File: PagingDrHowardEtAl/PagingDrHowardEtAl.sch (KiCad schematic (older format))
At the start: 0 parts

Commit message: Complete PagingDrHowardEtAl
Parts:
- added P1: Pulse Playground, ~, symbol CONN_3
- added P2: 7 segment backpack, ~, symbol CONN_5
- added P3: Bargraph Backpack, ~, symbol CONN_4
- added U1: ITSYBITSY, ~, symbol ITSYBITSY
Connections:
- new net +: P2.3, U1.30 (Vhi)
- new net -: P1.3 (P3), P2.4, P3.3 (P3), U1.2 (G)
- new net C: P2.2, P3.1 (P1), U1.11 (SCL/3)
- new net D: P2.1, P3.2 (P2), U1.12 (SDA/2)
- new net IO: P1.1 (P1), P2.5, P3.4 (P4), U1.32 (3V)
- new net Pulse: P1.2 (PM), U1.29 (A0)
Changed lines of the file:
@@
 LIBS:feather_m0_express
 LIBS:metromini
+LIBS:itsybitsy
+LIBS:PagingDrHowardEtAl-cache
 EELAYER 27 0
 EELAYER END
@@
 Sheet 1 1
 Title ""
-Date "22 oct 2018"
+Date "5 nov 2018"
 Rev ""
 Comp ""
@@
 Comment4 ""
 $EndDescr
+$Comp
+L CONN_3 P1
+U 1 1 5BE04B98
+P 2050 3100
+F 0 "P1" V 2000 3100 50  0000 C CNN
+F 1 "Pulse Playground" V 2100 3100 40  0000 C CNN
+F 2 "~" H 2050 3100 60  0000 C CNN
+F 3 "~" H 2050 3100 60  0000 C CNN
+	1    2050 3100
+	-1   0    0    -1
+$EndComp
+$Comp
+L CONN_4 P3
+U 1 1 5BE04C5D
+P 5300 3700
+F 0 "P3" V 5250 3700 50  0000 C CNN
+F 1 "Bargraph Backpack" V 5350 3700 50  0000 C CNN
+F 2 "~" H 5300 3700 60  0000 C CNN
+F 3 "~" H 5300 3700 60  0000 C CNN
+	1    5300 3700
+	1    0    0    -1
+$EndComp
+$Comp
+L CONN_5 P2
+U 1 1 5BE05043
+P 5300 2450
+F 0 "P2" V 5250 2450 50  0000 C CNN
+F 1 "7 segment backpack" V 5350 2450 50  0000 C CNN
+F 2 "~" H 5300 2450 60  0000 C CNN
+F 3 "~" H 5300 2450 60  0000 C CNN
+	1    5300 2450
+	1    0    0    -1
+$EndComp
+Text Label 4900 2250 2    60   ~ 0
+D
+Text Label 4900 2350 2    60   ~ 0
+C
+Text Label 4900 2450 2    60   ~ 0
++
+Text Label 4900 2550 2    60   ~ 0
+-
+Text Label 4900 2650 2    60   ~ 0
+IO
+Text Label 4950 3550 2    60   ~ 0
+SCL
+Text Label 4950 3650 2    60   ~ 0
+SDA
+Text Label 4950 3750 2    60   ~ 0
+G
+Text Label 4950 3850 2    60   ~ 0
+Vcc
+Text Label 2400 3000 0    60   ~ 0
+Vdd
+Text Label 2400 3100 0    60   ~ 0
+Pulse
+Text Label 2400 3200 0    60   ~ 0
+GND
+$Comp
+L ITSYBITSY U1
+U 1 1 5BE053A3
+P 3700 2600
+F 0 "U1" H 3700 2900 60  0000 C CNN
+F 1 "ITSYBITSY" H 3650 2200 60  0000 C CNN
+F 2 "~" H 3700 2600 60  0000 C CNN
+F 3 "~" H 3700 2600 60  0000 C CNN
+	1    3700 2600
+	0    1    1    0
+$EndComp
+Wire Wire Line
+	2400 3000 2600 3000
+Wire Wire Line
+	2600 1400 2600 4500
+Wire Wire Line
+	2600 1400 2950 1400
+Wire Wire Line
+	2400 3200 2500 3200
+Wire Wire Line
+	2500 3200 2500 650
+Wire Wire Line
+	2500 650  4650 650
+Wire Wire Line
+	4650 650  4650 1200
+Wire Wire Line
+	4650 1200 4400 1200
+Wire Wire Line
+	2400 3100 2700 3100
+Wire Wire Line
+	2700 3100 2700 1850
+Wire Wire Line
+	2700 1850 2950 1850
+Wire Wire Line
+	4900 2250 4650 2250
+Wire Wire Line
+	4650 2250 4650 3650
+Wire Wire Line
+	4650 2700 4400 2700
+Wire Wire Line
+	4650 3650 4950 3650
+Connection ~ 4650 2700
+Wire Wire Line
+	4900 2350 4750 2350
+Wire Wire Line
+	4750 2350 4750 3550
+Wire Wire Line
+	4750 2550 4400 2550
+Wire Wire Line
+	4750 3550 4950 3550
+Connection ~ 4750 2550
+Wire Wire Line
+	4950 3750 4550 3750
+Wire Wire Line
+	4550 3750 4550 1200
+Connection ~ 4550 1200
+Wire Wire Line
+	4900 2550 4800 2550
+Wire Wire Line
+	4800 2550 4800 2850
+Wire Wire Line
+	4800 2850 4550 2850
+Connection ~ 4550 2850
+Wire Wire Line
+	4900 2650 4900 3500
+Wire Wire Line
+	4900 3500 4350 3500
+Wire Wire Line
+	4350 3500 4350 4500
+Wire Wire Line
+	4350 4500 2600 4500
+Connection ~ 2600 3000
+Wire Wire Line
+	4950 3850 4350 3850
+Connection ~ 4350 3850
+Wire Wire Line
+	4900 2450 4700 2450
+Wire Wire Line
+	4700 2450 4700 750
+Wire Wire Line
+	4700 750  2800 750
+Wire Wire Line
+	2800 750  2800 1700
+Wire Wire Line
+	2800 1700 2950 1700
 $EndSCHEMATC

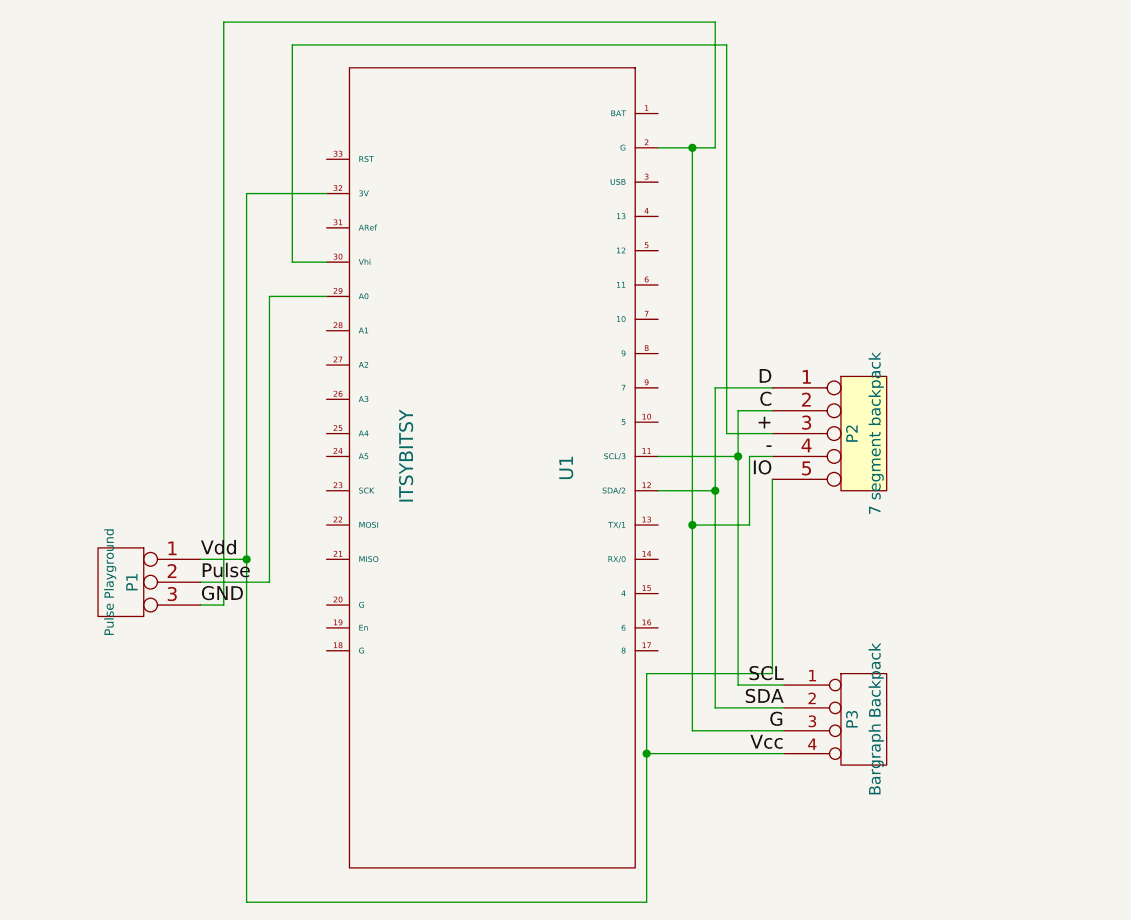
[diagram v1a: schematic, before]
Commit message: Add detailed comments to both the code and the schematics
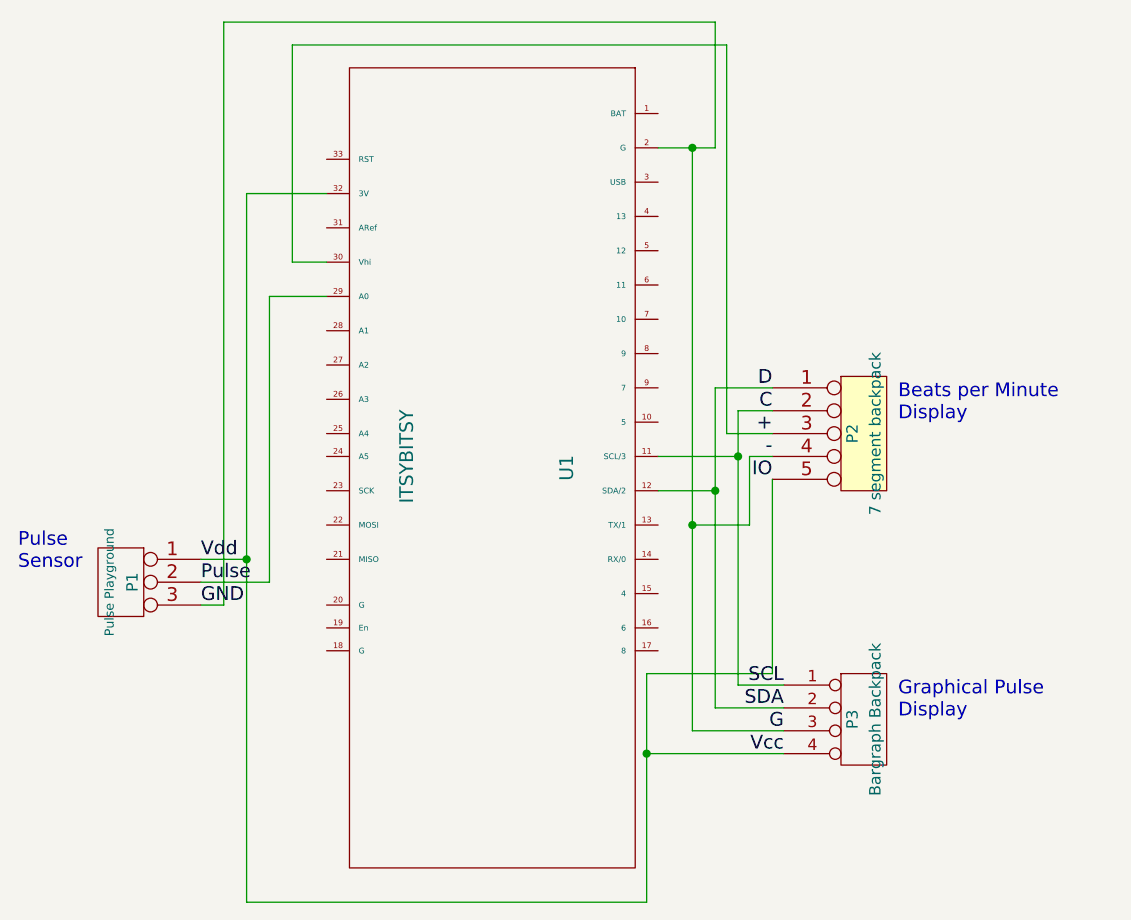
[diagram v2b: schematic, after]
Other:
- note added: "Beats per Minute\nDisplay"
- note added: "Graphical Pulse\nDisplay"
- note added: "Pulse\nSensor"
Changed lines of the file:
@@
 Sheet 1 1
 Title ""
-Date "5 nov 2018"
+Date "11 nov 2018"
 Rev ""
 Comp ""
@@
 Wire Wire Line
 	2800 1700 2950 1700
+Text Notes 1600 3050 0    60   ~ 0
+Pulse\nSensor
+Text Notes 5450 2400 0    60   ~ 0
+Beats per Minute\nDisplay
+Text Notes 5450 3700 0    60   ~ 0
+Graphical Pulse\nDisplay
 $EndSCHEMATC

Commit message: Update PagingDrHowardEtAl.
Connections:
- net +: now also U1.32 (3V); no longer U1.30 (Vhi)
- net -: now also U1.18 (G), U1.30 (Vhi)
- net IO: now also U1.20 (G); no longer U1.32 (3V)
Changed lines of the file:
@@
 Sheet 1 1
 Title ""
-Date "11 nov 2018"
+Date "27 aug 2019"
 Rev ""
 Comp ""
@@
 	2400 3000 2600 3000
 Wire Wire Line
-	2600 1400 2600 4500
-Wire Wire Line
-	2600 1400 2950 1400
-Wire Wire Line
 	2400 3200 2500 3200
 Wire Wire Line
@@
 Connection ~ 4750 2550
 Wire Wire Line
-	4950 3750 4550 3750
+	4550 3750 4950 3750
 Wire Wire Line
-	4550 3750 4550 1200
+	4550 1200 4550 3750
 Connection ~ 4550 1200
 Wire Wire Line
@@
 	4900 2450 4700 2450
 Wire Wire Line
-	4700 2450 4700 750
-Wire Wire Line
-	4700 750  2800 750
-Wire Wire Line
-	2800 750  2800 1700
-Wire Wire Line
 	2800 1700 2950 1700
 Text Notes 1600 3050 0    60   ~ 0
@@
 Text Notes 5450 3700 0    60   ~ 0
 Graphical Pulse\nDisplay
+Wire Wire Line
+	2600 3200 2950 3200
+Connection ~ 2600 3200
+Wire Wire Line
+	2800 650  2800 3400
+Wire Wire Line
+	2800 3400 2950 3400
+Connection ~ 2800 650
+Connection ~ 2800 1700
+Wire Wire Line
+	2600 4500 2600 3000
+Wire Wire Line
+	4700 2450 4700 800
+Wire Wire Line
+	4700 800  2850 800
+Wire Wire Line
+	2850 800  2850 1450
+Wire Wire Line
+	2850 1450 2950 1450
+Wire Wire Line
+	2950 1450 2950 1400
 $EndSCHEMATC

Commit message: Revert "Update PagingDrHowardEtAl."
This reverts commit db79b4fbad0fb7acf435444e0c859a0f028222a4.
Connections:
- net +: now also U1.30 (Vhi); no longer U1.32 (3V)
- net -: no longer U1.18 (G), U1.30 (Vhi)
- net IO: now also U1.32 (3V); no longer U1.20 (G)
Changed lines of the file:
@@
 Sheet 1 1
 Title ""
-Date "27 aug 2019"
+Date "11 nov 2018"
 Rev ""
 Comp ""
@@
 	2400 3000 2600 3000
 Wire Wire Line
+	2600 1400 2600 4500
+Wire Wire Line
+	2600 1400 2950 1400
+Wire Wire Line
 	2400 3200 2500 3200
 Wire Wire Line
@@
 Connection ~ 4750 2550
 Wire Wire Line
-	4550 3750 4950 3750
+	4950 3750 4550 3750
 Wire Wire Line
-	4550 1200 4550 3750
+	4550 3750 4550 1200
 Connection ~ 4550 1200
 Wire Wire Line
@@
 	4900 2450 4700 2450
 Wire Wire Line
+	4700 2450 4700 750
+Wire Wire Line
+	4700 750  2800 750
+Wire Wire Line
+	2800 750  2800 1700
+Wire Wire Line
 	2800 1700 2950 1700
 Text Notes 1600 3050 0    60   ~ 0
@@
 Text Notes 5450 3700 0    60   ~ 0
 Graphical Pulse\nDisplay
-Wire Wire Line
-	2600 3200 2950 3200
-Connection ~ 2600 3200
-Wire Wire Line
-	2800 650  2800 3400
-Wire Wire Line
-	2800 3400 2950 3400
-Connection ~ 2800 650
-Connection ~ 2800 1700
-Wire Wire Line
-	2600 4500 2600 3000
-Wire Wire Line
-	4700 2450 4700 800
-Wire Wire Line
-	4700 800  2850 800
-Wire Wire Line
-	2850 800  2850 1450
-Wire Wire Line
-	2850 1450 2950 1450
-Wire Wire Line
-	2950 1450 2950 1400
 $EndSCHEMATC

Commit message: Corrected version of PagingDrHowardEtA.
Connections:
- net + renamed +5V
- net +5V: now also P2.4; no longer P2.3
- net - renamed G
- net G: now also P2.3; no longer P2.4
- net C renamed SCL
- net SCL: now also P2.1; no longer P2.2
- net D renamed SDA
- net SDA: now also P2.2; no longer P2.1
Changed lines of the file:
@@
 $EndComp
 Text Label 4900 2250 2    60   ~ 0
-D
+SCL
 Text Label 4900 2350 2    60   ~ 0
-C
+SDA
 Text Label 4900 2450 2    60   ~ 0
-+
+GND
 Text Label 4900 2550 2    60   ~ 0
--
++5V
 Text Label 4900 2650 2    60   ~ 0
 IO
@@
 	2700 1850 2950 1850
 Wire Wire Line
-	4900 2250 4650 2250
-Wire Wire Line
-	4650 2250 4650 3650
-Wire Wire Line
 	4650 2700 4400 2700
 Wire Wire Line
@@
 Connection ~ 4650 2700
 Wire Wire Line
-	4900 2350 4750 2350
-Wire Wire Line
-	4750 2350 4750 3550
+	4750 2250 4750 3550
 Wire Wire Line
 	4750 2550 4400 2550
@@
 	4550 3750 4550 1200
 Connection ~ 4550 1200
-Wire Wire Line
-	4900 2550 4800 2550
-Wire Wire Line
-	4800 2550 4800 2850
-Wire Wire Line
-	4800 2850 4550 2850
-Connection ~ 4550 2850
 Wire Wire Line
 	4900 2650 4900 3500
@@
 Connection ~ 4350 3850
 Wire Wire Line
-	4900 2450 4700 2450
-Wire Wire Line
-	4700 2450 4700 750
+	4700 750  4700 2650
 Wire Wire Line
 	4700 750  2800 750
@@
 Wire Wire Line
 	2600 1400 2950 1400
+Wire Wire Line
+	4750 2250 4900 2250
+Wire Wire Line
+	4900 2350 4650 2350
+Wire Wire Line
+	4650 2350 4650 3650
+Wire Wire Line
+	4700 2650 4800 2650
+Wire Wire Line
+	4800 2650 4800 2550
+Wire Wire Line
+	4800 2550 4900 2550
+Wire Wire Line
+	4900 2450 4550 2450
+Connection ~ 4550 2450
 $EndSCHEMATC

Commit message: PagingDrHowardEtAl, using an UNO R3
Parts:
- removed U1: ITSYBITSY, ~, symbol ITSYBITSY
- added U1: UNO, ~, symbol UNO
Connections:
- net +5V: now also P2.5, P3.4 (P4), U1.5V (+5V)
- net G: now also U1.G (GND)
- net Pulse: now also U1.A0
- net SCL: now also U1.SCL (SCL_(A5))
- net SDA: now also U1.SDA (SDA_(A4))
- removed net IO: P1.1 (P1), P2.5, P3.4 (P4)
- new net Vdd: P1.1 (P1), U1.3V (+3V), U1.AREF (ARef)
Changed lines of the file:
@@
 LIBS:metromini
 LIBS:itsybitsy
+LIBS:uno
 LIBS:PagingDrHowardEtAl-cache
 EELAYER 27 0
@@
 Sheet 1 1
 Title ""
-Date "27 aug 2019"
+Date "28 aug 2019"
 Rev ""
 Comp ""
@@
 Text Label 2400 3200 0    60   ~ 0
 GND
-$Comp
-L ITSYBITSY U1
-U 1 1 5BE053A3
-P 3700 2600
-F 0 "U1" H 3700 2900 60  0000 C CNN
-F 1 "ITSYBITSY" H 3650 2200 60  0000 C CNN
-F 2 "~" H 3700 2600 60  0000 C CNN
-F 3 "~" H 3700 2600 60  0000 C CNN
-	1    3700 2600
-	0    1    1    0
-$EndComp
 Wire Wire Line
 	2400 3000 2600 3000
 Wire Wire Line
-	2600 1400 2600 4500
+	2400 3200 4550 3200
 Wire Wire Line
-	2400 3200 2500 3200
-Wire Wire Line
-	2500 3200 2500 650
-Wire Wire Line
-	2500 650  4650 650
-Wire Wire Line
-	4650 650  4650 1200
-Wire Wire Line
-	4650 1200 4400 1200
-Wire Wire Line
-	2400 3100 2700 3100
-Wire Wire Line
-	2700 3100 2700 1850
-Wire Wire Line
-	2700 1850 2950 1850
-Wire Wire Line
-	4650 2700 4400 2700
+	2400 3100 4400 3100
 Wire Wire Line
 	4650 3650 4950 3650
-Connection ~ 4650 2700
 Wire Wire Line
 	4750 2250 4750 3550
 Wire Wire Line
-	4750 2550 4400 2550
-Wire Wire Line
 	4750 3550 4950 3550
-Connection ~ 4750 2550
 Wire Wire Line
 	4950 3750 4550 3750
 Wire Wire Line
-	4550 3750 4550 1200
-Connection ~ 4550 1200
+	4900 3500 4900 2550
 Wire Wire Line
-	4900 2650 4900 3500
-Wire Wire Line
-	4900 3500 4350 3500
-Wire Wire Line
-	4350 3500 4350 4500
-Wire Wire Line
-	4350 4500 2600 4500
-Connection ~ 2600 3000
+	2800 3500 4900 3500
 Wire Wire Line
 	4950 3850 4350 3850
-Connection ~ 4350 3850
-Wire Wire Line
-	4700 750  4700 2650
-Wire Wire Line
-	4700 750  2800 750
-Wire Wire Line
-	2800 750  2800 1700
 Text Notes 1600 3050 0    60   ~ 0
 Pulse\nSensor
@@
 Graphical Pulse\nDisplay
 Wire Wire Line
-	2800 1700 2950 1700
-Wire Wire Line
-	2600 1400 2950 1400
-Wire Wire Line
 	4750 2250 4900 2250
 Wire Wire Line
@@
 	4650 2350 4650 3650
 Wire Wire Line
-	4700 2650 4800 2650
+	4900 2450 4550 2450
+Connection ~ 4900 2650
 Wire Wire Line
-	4800 2650 4800 2550
+	4550 2450 4550 3750
 Wire Wire Line
-	4800 2550 4900 2550
+	4350 3850 4350 3500
+Connection ~ 4550 3200
+$Comp
+L UNO U1
+U 1 1 5D66D46F
+P 3500 2500
+F 0 "U1" H 3500 2700 60  0000 C CNN
+F 1 "UNO" H 3550 2550 60  0000 C CNN
+F 2 "~" H 3500 2500 60  0000 C CNN
+F 3 "~" H 3500 2500 60  0000 C CNN
+	1    3500 2500
+	1    0    0    -1
+$EndComp
 Wire Wire Line
-	4900 2450 4550 2450
-Connection ~ 4550 2450
+	4400 3100 4400 2350
+Wire Wire Line
+	4400 2350 4000 2350
+Wire Wire Line
+	4000 2200 4000 1750
+Wire Wire Line
+	4000 1750 2350 1750
+Wire Wire Line
+	2350 1750 2350 2300
+Wire Wire Line
+	2350 2300 2950 2300
+Wire Wire Line
+	2600 3000 2600 2300
+Connection ~ 2600 2300
+Wire Wire Line
+	2800 3500 2800 2200
+Wire Wire Line
+	2800 2200 2950 2200
+Connection ~ 4350 3500
+Wire Wire Line
+	2950 2400 2950 3200
+Connection ~ 2950 3200
+Wire Wire Line
+	4000 2650 4750 2650
+Connection ~ 4750 2650
+Wire Wire Line
+	4000 2550 4650 2550
+Connection ~ 4650 2550
 $EndSCHEMATC
